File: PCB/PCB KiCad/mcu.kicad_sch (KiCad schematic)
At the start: 9 parts

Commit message: first check + add connectors
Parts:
- added J?: Qwiic, symbol Connector_Generic:Conn_01x04
- added J?: ADC Debug, symbol Connector_Generic:Conn_01x08
- added J?: LED Debug, symbol Connector_Generic:Conn_01x04
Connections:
- net +3V3: now also J?.2 (Pin_2)
- net ADC DRDY: now also J?.6 (Pin_6)
- net ADC PDWN: now also J?.8 (Pin_8)
- net ADC RESET: now also J?.7 (Pin_7)
- net GND: now also J?.1 (Pin_1), J?.1 (Pin_1), J?.1 (Pin_1)
- net I2C_SCL: now also J?.3 (Pin_3), J?.4 (Pin_4)
- net I2C_SDA: now also J?.2 (Pin_2), J?.3 (Pin_3)
- net LED RESET: now also J?.4 (Pin_4)
- net SPI_CLK: now also J?.5 (Pin_5)
- net SPI_CS: now also J?.2 (Pin_2)
- net SPI_MISO: now also J?.4 (Pin_4)
- net SPI_MOSI: now also J?.3 (Pin_3)
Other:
- note added: "Connectors"

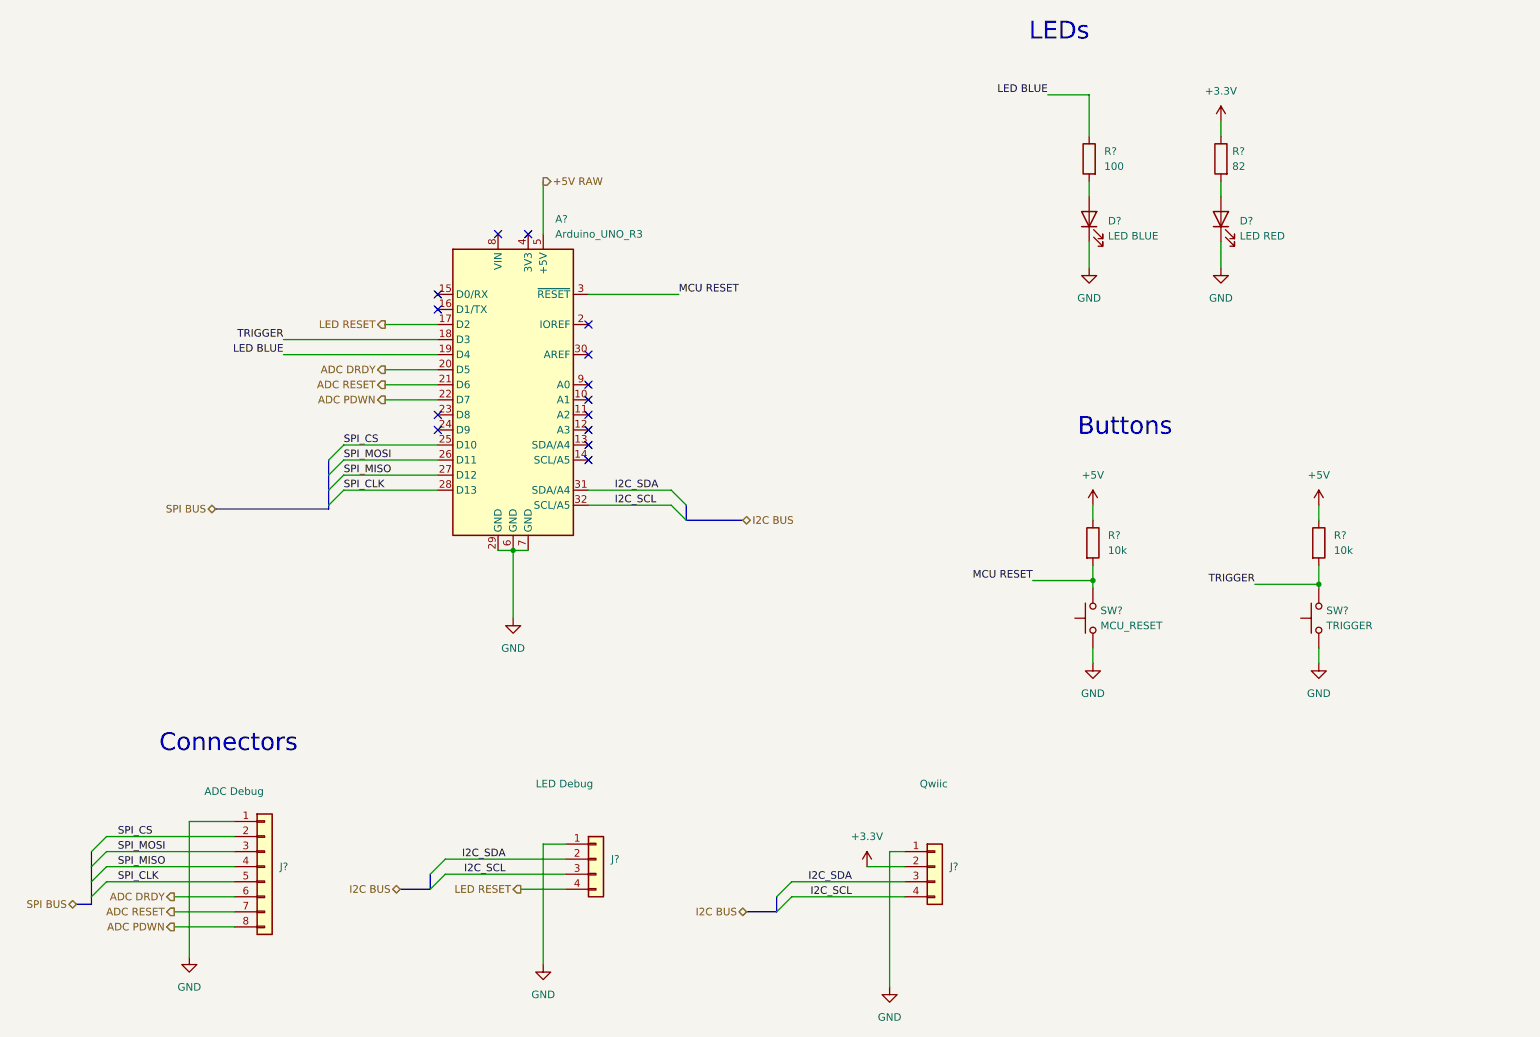
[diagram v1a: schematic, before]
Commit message: ERC: add power flags to satisfy the ERC crap
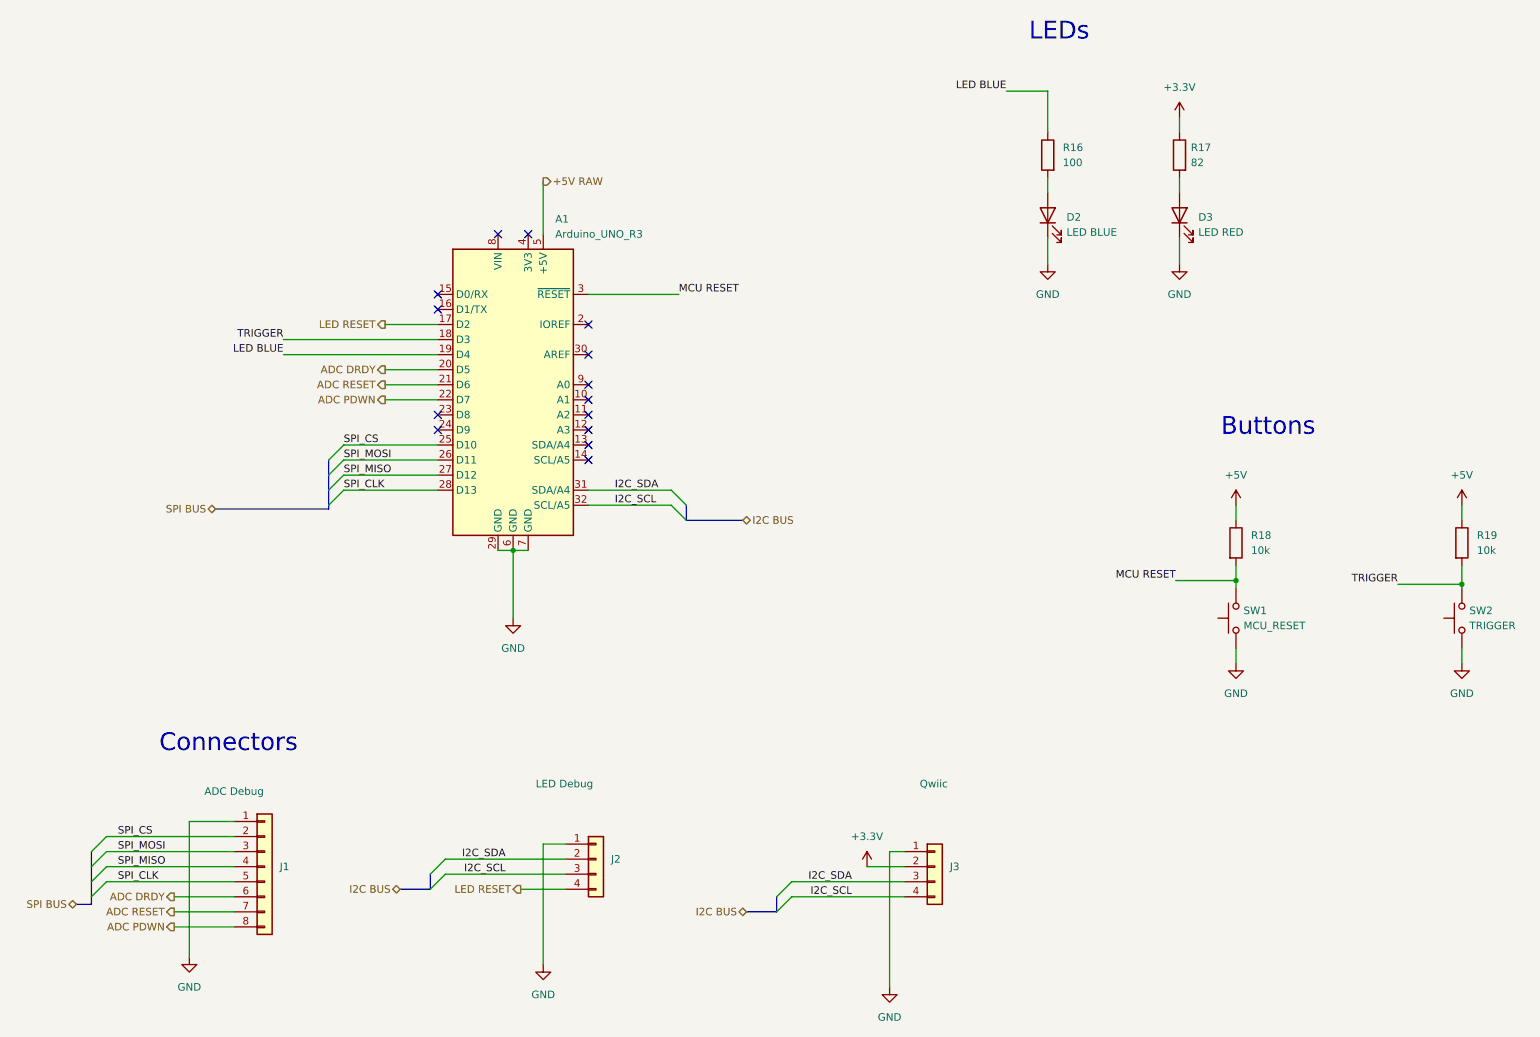
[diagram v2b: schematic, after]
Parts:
- gave numbers to parts that had none: 12
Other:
- moved on the sheet: D2, D3, R16, R17, R18, R19, SW1, SW2

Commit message: Satisfy the overdemanding attention hungry ERC monster
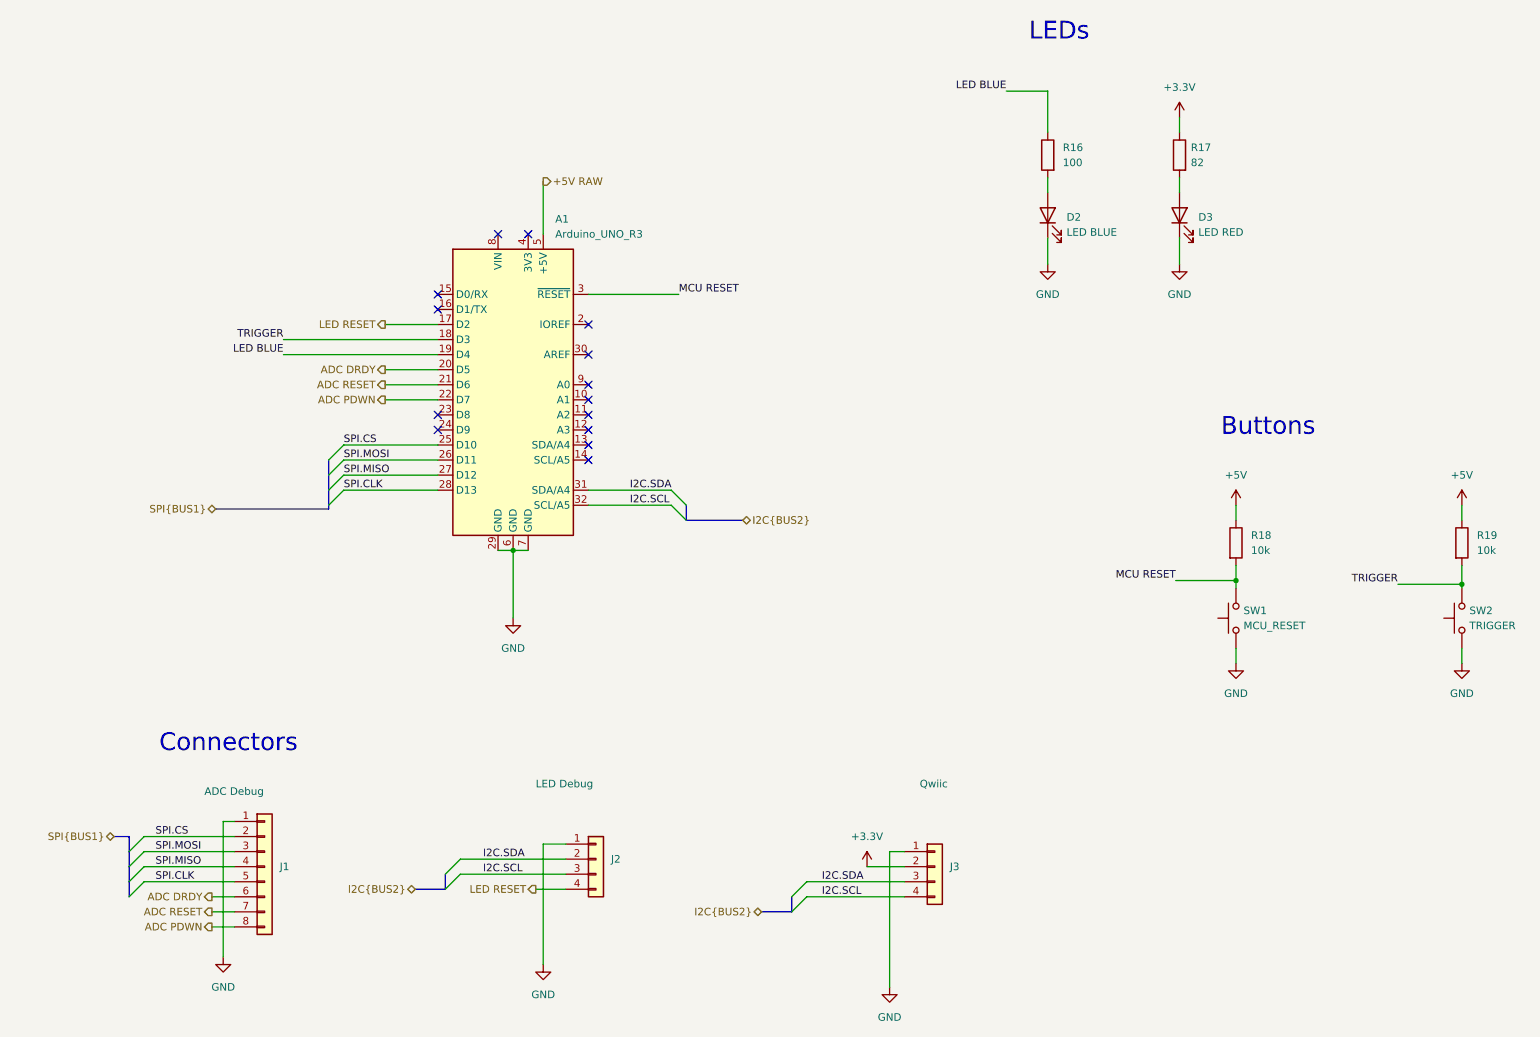
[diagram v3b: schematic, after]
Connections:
- net I2C_SCL renamed I2C.SCL
- net I2C_SDA renamed I2C.SDA
- net SPI_CLK renamed SPI.CLK
- net SPI_CS renamed SPI.CS
- net SPI_MISO renamed SPI.MISO
- net SPI_MOSI renamed SPI.MOSI

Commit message: Add footprints
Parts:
- D2, D3: footprint (none) -> LED_SMD:LED_0805_2012Metric_Pad1.15x1.40mm_HandSolder
- J1: footprint (none) -> Connector_PinHeader_2.54mm:PinHeader_1x08_P2.54mm_Vertical
- J2: footprint (none) -> Connector_PinHeader_2.54mm:PinHeader_1x04_P2.54mm_Vertical
- R16, R17, R18, R19: footprint (none) -> Resistor_SMD:R_0805_2012Metric_Pad1.20x1.40mm_HandSolder
- SW1, SW2: footprint (none) -> Button_Switch_THT:SW_PUSH_6mm_H4.3mm
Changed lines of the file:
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@@
       (effects (font (size 1.27 1.27)) (justify right))
     )
-    (property "Footprint" "" (id 2) (at 211.455 57.785 0)
+    (property "Footprint" "LED_SMD:LED_0805_2012Metric_Pad1.15x1.40mm_HandSolder" (id 2) (at 211.455 57.785 0)
       (effects (font (size 1.27 1.27)) hide)
     )
@@
       (effects (font (size 1.27 1.27)) (justify right))
     )
-    (property "Footprint" "" (id 2) (at 215.9 125.73 0)
+    (property "Footprint" "Button_Switch_THT:SW_PUSH_6mm_H4.3mm" (id 2) (at 215.9 125.73 0)
       (effects (font (size 1.27 1.27)) hide)
     )
@@
       (effects (font (size 1.27 1.27)) (justify left))
     )
-    (property "Footprint" "" (id 2) (at 257.302 113.03 90)
+    (property "Footprint" "Resistor_SMD:R_0805_2012Metric_Pad1.20x1.40mm_HandSolder" (id 2) (at 257.302 113.03 90)
       (effects (font (size 1.27 1.27)) hide)
     )
@@
       (effects (font (size 1.27 1.27)) (justify right))
     )
-    (property "Footprint" "" (id 2) (at 191.008 47.625 90)
+    (property "Footprint" "Resistor_SMD:R_0805_2012Metric_Pad1.20x1.40mm_HandSolder" (id 2) (at 191.008 47.625 90)
       (effects (font (size 1.27 1.27)) hide)
     )
@@
       (effects (font (size 1.27 1.27)) (justify right))
     )
-    (property "Footprint" "" (id 2) (at 254 125.73 0)
+    (property "Footprint" "Button_Switch_THT:SW_PUSH_6mm_H4.3mm" (id 2) (at 254 125.73 0)
       (effects (font (size 1.27 1.27)) hide)
     )
@@
       (effects (font (size 1.27 1.27)) (justify right))
     )
-    (property "Footprint" "" (id 2) (at 213.233 47.625 90)
+    (property "Footprint" "Resistor_SMD:R_0805_2012Metric_Pad1.20x1.40mm_HandSolder" (id 2) (at 213.233 47.625 90)
       (effects (font (size 1.27 1.27)) hide)
     )
@@
       (effects (font (size 1.27 1.27)) (justify right))
     )
-    (property "Footprint" "" (id 2) (at 189.23 57.785 0)
+    (property "Footprint" "LED_SMD:LED_0805_2012Metric_Pad1.15x1.40mm_HandSolder" (id 2) (at 189.23 57.785 0)
       (effects (font (size 1.27 1.27)) hide)
     )
@@
       (effects (font (size 1.27 1.27)) (justify left))
     )
-    (property "Footprint" "" (id 2) (at 57.15 167.64 0)
+    (property "Footprint" "Connector_PinHeader_2.54mm:PinHeader_1x08_P2.54mm_Vertical" (id 2) (at 57.15 167.64 0)
       (effects (font (size 1.27 1.27)) hide)
     )
@@
       (effects (font (size 1.27 1.27)) (justify left))
     )
-    (property "Footprint" "" (id 2) (at 219.202 113.03 90)
+    (property "Footprint" "Resistor_SMD:R_0805_2012Metric_Pad1.20x1.40mm_HandSolder" (id 2) (at 219.202 113.03 90)
       (effects (font (size 1.27 1.27)) hide)
     )
@@
       (effects (font (size 1.27 1.27)) (justify left))
     )
-    (property "Footprint" "" (id 2) (at 113.03 166.37 0)
-      (effects (font (size 1.27 1.27)) hide)
-    )
+    (property "Footprint" "Connector_PinHeader_2.54mm:PinHeader_1x04_P2.54mm_Vertical" (id 2) (at 113.03 166.37 0)
+      (effects (font (size 1.27 1.27)) hide)
+    )

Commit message: Added missing footprint symbols
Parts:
- J3: footprint (none) -> Connector_JST:JST_SH_SM04B-SRSS-TB_1x04-1MP_P1.00mm_Horizontal
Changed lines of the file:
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@@
       (effects (font (size 1.27 1.27)) (justify left))
     )
-    (property "Footprint" "" (id 2) (at 170.18 167.64 0)
+    (property "Footprint" "Connector_JST:JST_SH_SM04B-SRSS-TB_1x04-1MP_P1.00mm_Horizontal" (id 2) (at 170.18 167.64 0)
       (effects (font (size 1.27 1.27)) hide)
     )

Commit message: placement of components
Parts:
- SW1, SW2: footprint Button_Switch_THT:SW_PUSH_6mm_H4.3mm -> Button_Switch_THT:SW_PUSH_6mm
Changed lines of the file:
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@@
       (effects (font (size 1.27 1.27)) (justify right))
     )
-    (property "Footprint" "Button_Switch_THT:SW_PUSH_6mm_H4.3mm" (id 2) (at 215.9 125.73 0)
+    (property "Footprint" "Button_Switch_THT:SW_PUSH_6mm" (id 2) (at 215.9 125.73 0)
       (effects (font (size 1.27 1.27)) hide)
     )
@@
       (effects (font (size 1.27 1.27)) (justify right))
     )
-    (property "Footprint" "Button_Switch_THT:SW_PUSH_6mm_H4.3mm" (id 2) (at 254 125.73 0)
+    (property "Footprint" "Button_Switch_THT:SW_PUSH_6mm" (id 2) (at 254 125.73 0)
       (effects (font (size 1.27 1.27)) hide)
     )

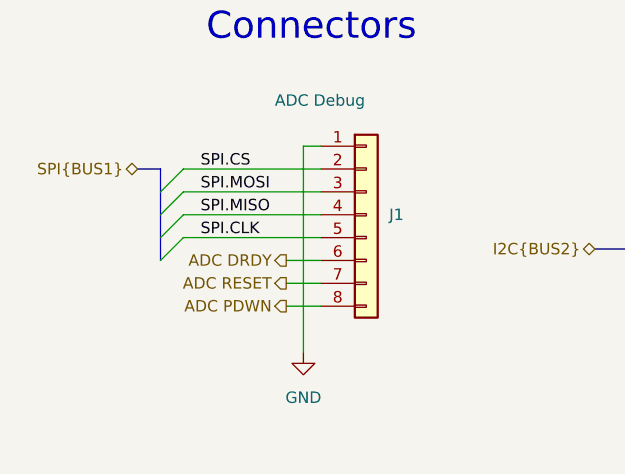
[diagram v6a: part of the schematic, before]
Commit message: routing: swap order of J1 ADC signals, swap buttons order
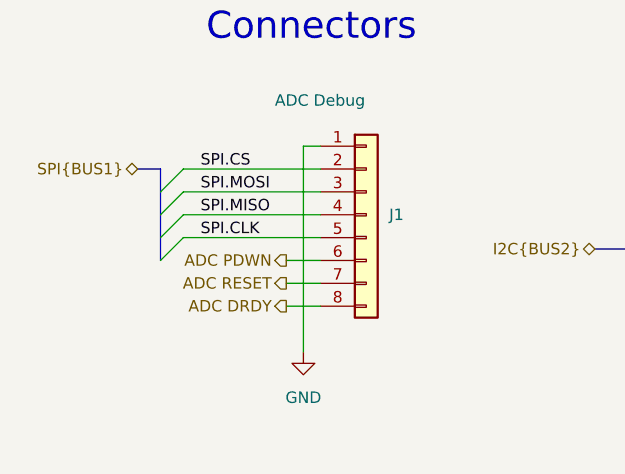
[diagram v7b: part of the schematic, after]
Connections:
- net ADC DRDY: now also J1.8 (Pin_8); no longer J1.6 (Pin_6)
- net ADC PDWN: now also J1.6 (Pin_6); no longer J1.8 (Pin_8)
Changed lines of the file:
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@@
     (effects (font (size 1.27 1.27)) (justify left bottom))
   )
-  (hierarchical_label "ADC PDWN" (shape output) (at 48.26 177.8 180)
-    (effects (font (size 1.27 1.27)) (justify right))
-  )
   (hierarchical_label "ADC RESET" (shape output) (at 77.47 86.36 180)
-    (effects (font (size 1.27 1.27)) (justify right))
-  )
-  (hierarchical_label "ADC DRDY" (shape output) (at 48.26 172.72 180)
     (effects (font (size 1.27 1.27)) (justify right))
   )
@@
     (effects (font (size 1.27 1.27)) (justify right))
   )
+  (hierarchical_label "ADC PDWN" (shape output) (at 48.26 172.72 180)
+    (effects (font (size 1.27 1.27)) (justify right))
+  )
   (hierarchical_label "I2C{BUS2}" (shape bidirectional) (at 82.55 171.45 180)
+    (effects (font (size 1.27 1.27)) (justify right))
+  )
+  (hierarchical_label "ADC RESET" (shape output) (at 48.26 175.26 180)
     (effects (font (size 1.27 1.27)) (justify right))
   )
@@
     (effects (font (size 1.27 1.27)) (justify right))
   )
-  (hierarchical_label "ADC RESET" (shape output) (at 48.26 175.26 180)
+  (hierarchical_label "ADC DRDY" (shape output) (at 48.26 177.8 180)
     (effects (font (size 1.27 1.27)) (justify right))
   )

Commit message: export for review
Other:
- company: (none) -> Plastic Scanner
- title: (none) -> Development Board
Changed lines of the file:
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@@
 (kicad_sch (version 20211123) (generator eeschema)
   (paper "A4")
+  (title_block
+    (title "Development Board")
+    (date "2022-03-15")
+    (rev "2.1")
+    (company "Plastic Scanner")
+  )
   (bus_alias "BUS2" (members "SDA" "SCL"))
   (junction (at 99.06 114.3) (diameter 0) (color 0 0 0 0)
